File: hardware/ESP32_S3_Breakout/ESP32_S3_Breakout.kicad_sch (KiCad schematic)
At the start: 25 parts, among them J1 USB_C_Receptacle_USB2.0, J2 Conn_01x20_Pin, J3 Conn_01x20_Pin, Q1 2N7002DW, SW1 SW_DPDT_x2, SW2 RESET, SW3 BOOT, U1 ESP32-S3-WROOM, U2 USBLC6-2P6, U3 CH340G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

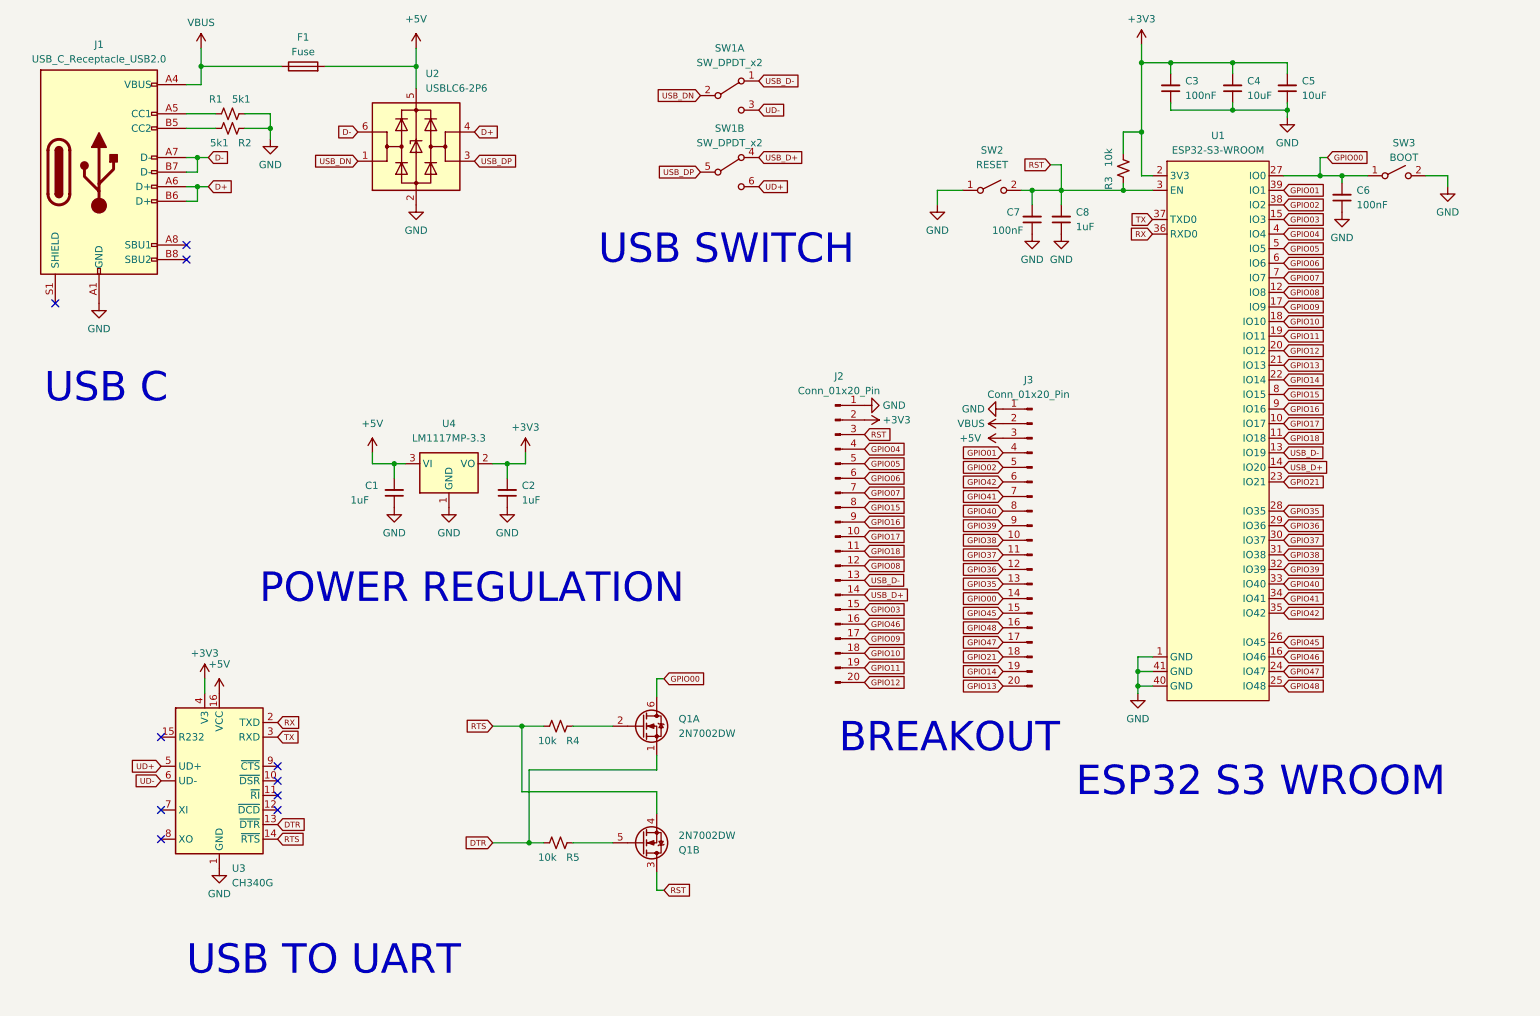
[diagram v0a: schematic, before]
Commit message: Version 02 - Added LEDs
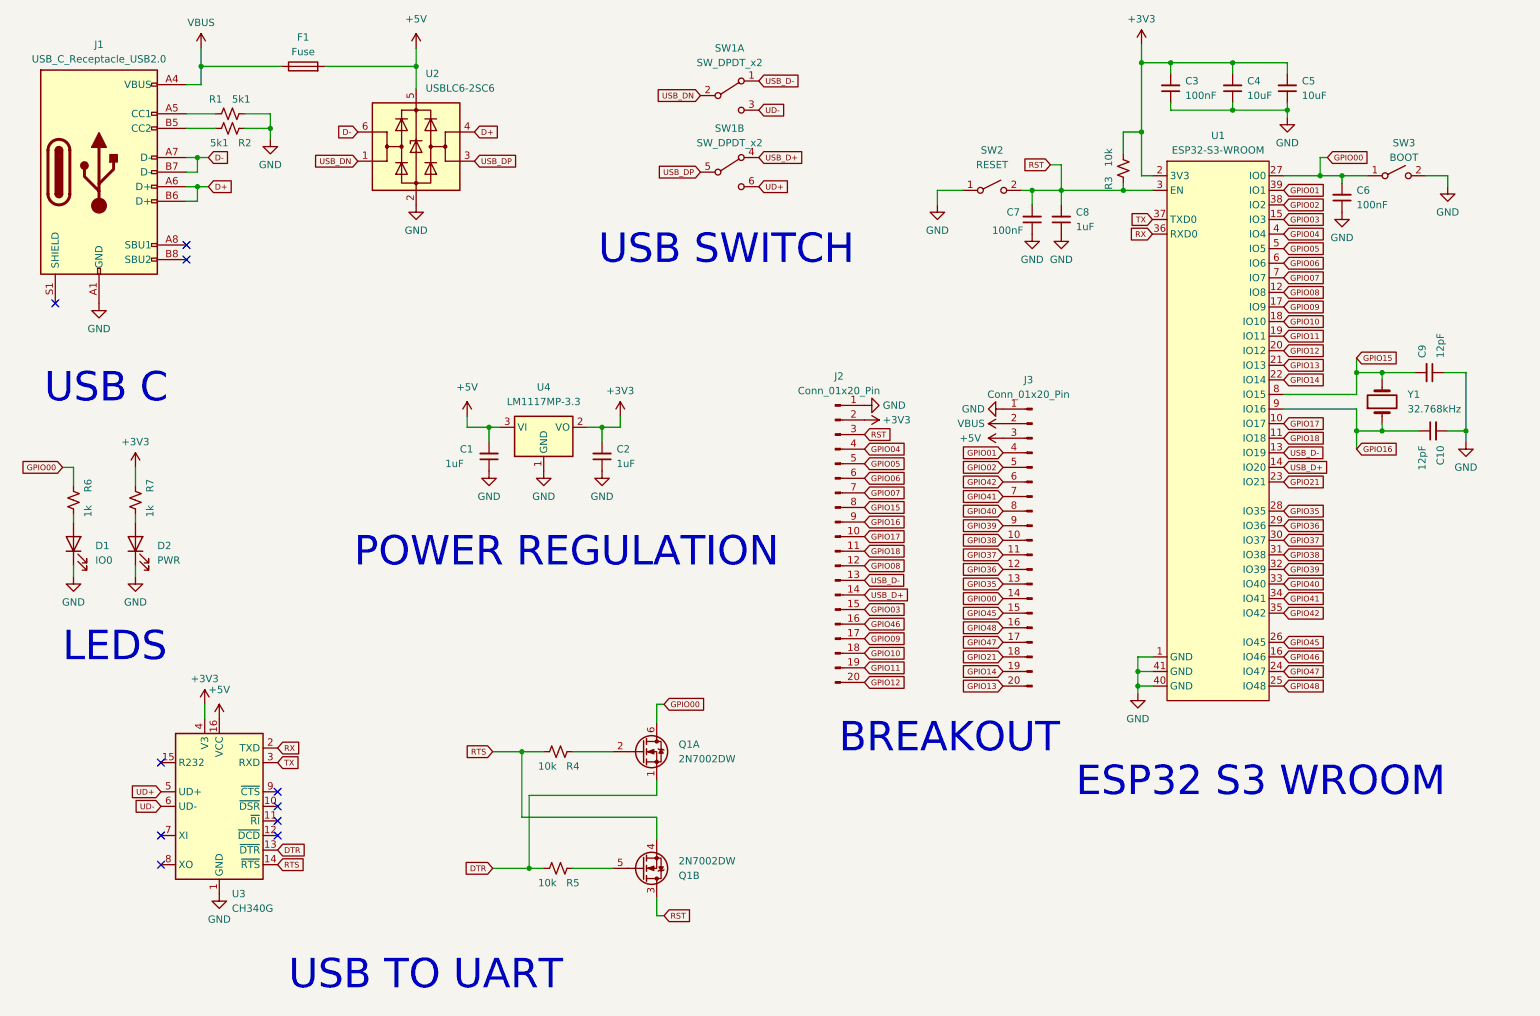
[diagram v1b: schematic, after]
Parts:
- removed U2: USBLC6-2P6, Package_TO_SOT_SMD:SOT-666, symbol Power_Protection:USBLC6-2P6
- added C10, C9: 12pF, Capacitor_SMD:C_0603_1608Metric, symbol Device:C_Small
- added D1: IO0, LED_SMD:LED_0603_1608Metric, symbol Device:LED
- added D2: PWR, LED_SMD:LED_0603_1608Metric, symbol Device:LED
- added R6, R7: 1k, Resistor_SMD:R_0603_1608Metric, symbol Device:R_Small_US
- added U2: USBLC6-2SC6, Package_TO_SOT_SMD:SOT-23-6, symbol Power_Protection:USBLC6-2SC6
- added Y1: 32.768kHz, Crystal:Crystal_SMD_EuroQuartz_EQ161-2Pin_3.2x1.5mm_HandSoldering, symbol Device:Crystal
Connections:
- net +3V3: now also R7.1
- net +5V: now also U2.5 (VBUS)
- net D+: now also U2.4 (I/O2)
- net D-: now also U2.6 (I/O1)
- net GND: now also C10.2, C9.1, D1.1 (K), D2.1 (K), U2.2 (GND)
- net GPIO00: now also R6.1
- net GPIO15: now also C9.2, Y1.2
- net GPIO16: now also C10.1, Y1.1
- net USB_DN: now also U2.1 (I/O1)
- net USB_DP: now also U2.3 (I/O2)
- new net: D2.2 (A), R7.2
- new net: D1.2 (A), R6.2
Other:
- note added: "LEDS"
- moved on the sheet: C1, C2, Q1A, Q1B, R4, R5, U3, U4
